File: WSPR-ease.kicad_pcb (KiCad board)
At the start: 4 copper layers, 99 x 64 mm, 113 parts, among them J1 GNSS Ant, J2 Tx Ant, J3 USB_C_16P_Stacked, Q1 MMBF170, Q10 MMBF170, Q11 MMBF170, Q12 MMBF170, Q13 MMBF170, Q2 MMBF170, Q3 MMBF170, Q4 MMBF170, Q5 MMBF170, Q6 MMBF170, Q7 MMBF170, Q8 MMBF170, Q9 MMBF170, T1 BN-43-202_DualPri_CTSec, U1 ESP32-S3-WROOM-1-N8R8, U2 NCP1117-3.3_SOT223, U3 ATGM336H-5N31, U4 ICE40UP5K-SG48ITR, U5 TLV70012, U6 CD74ACT541SM96, U7 SRV05-4

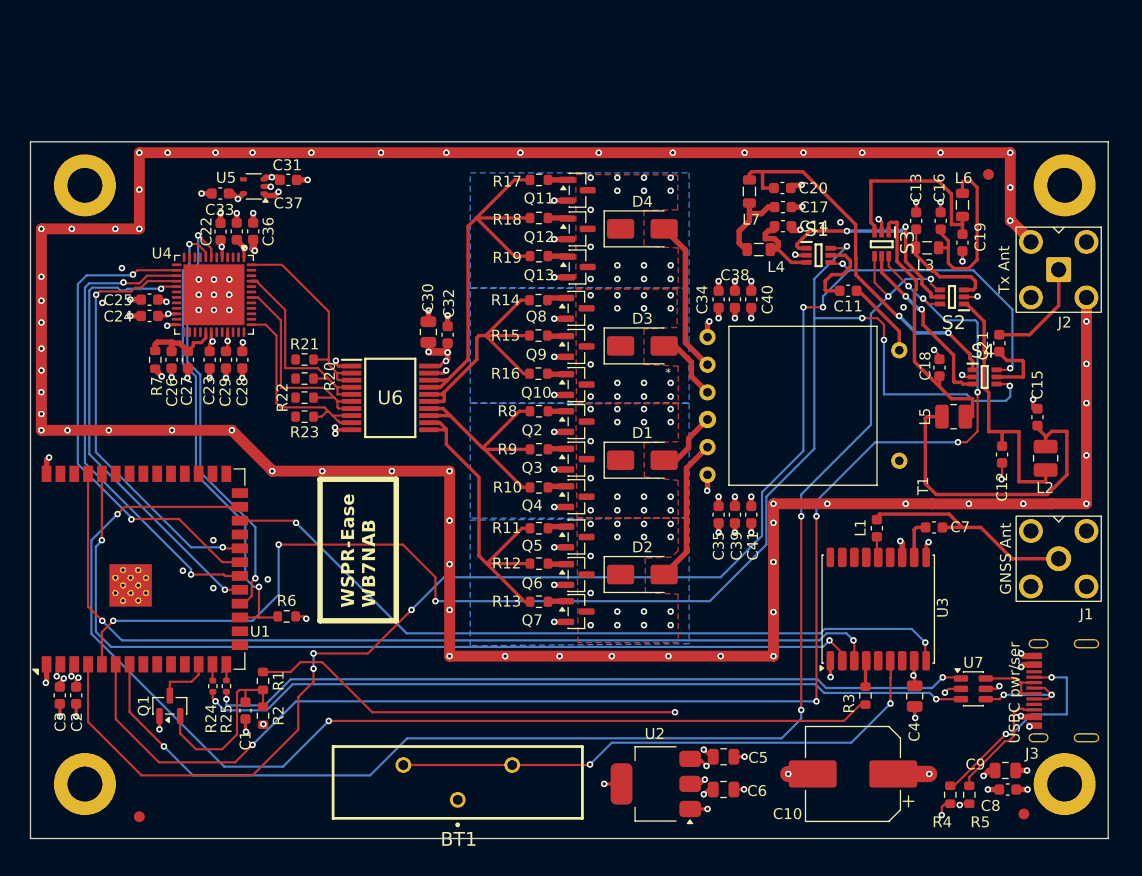
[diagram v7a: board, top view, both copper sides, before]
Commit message: Tarted up, 3d models applied, better footprints and BOM, ready to submit for PCBA
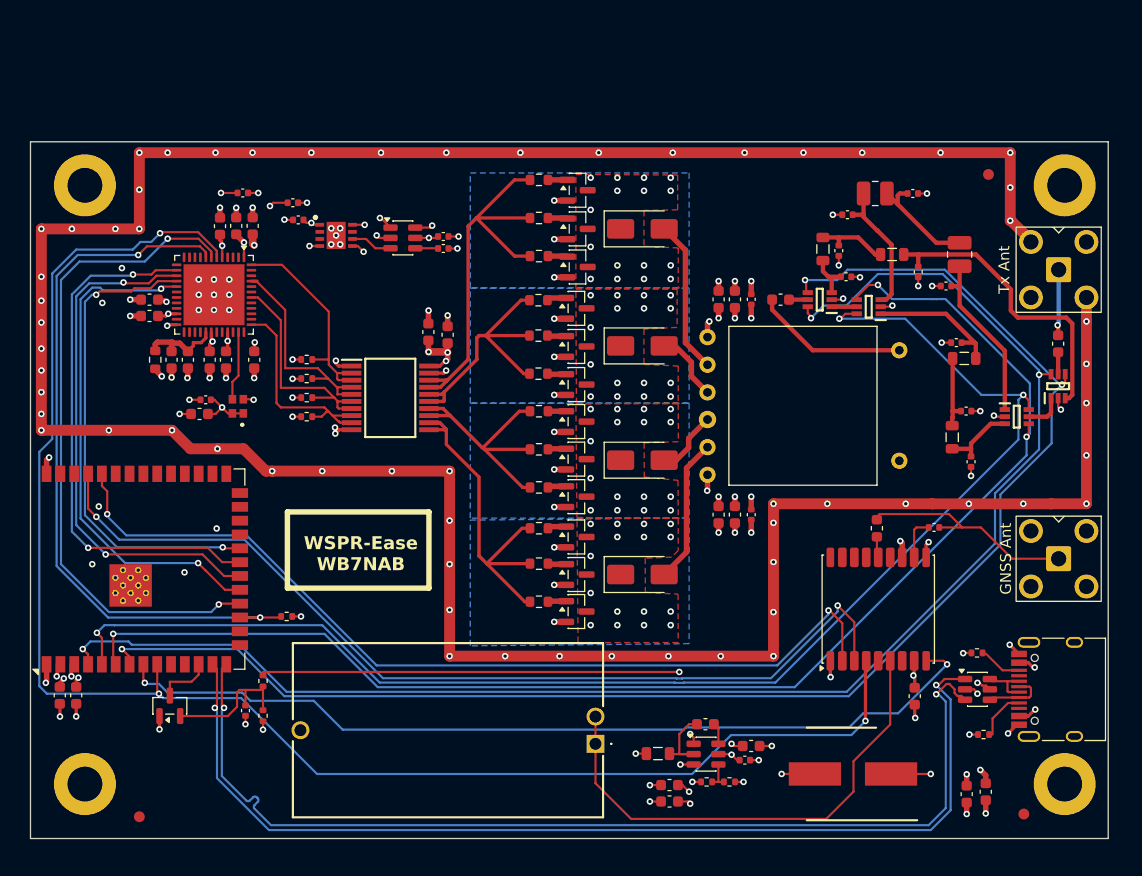
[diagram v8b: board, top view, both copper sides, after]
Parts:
- removed C31, C33: 1uF X7R 25V, Capacitor_SMD:C_0603_1608Metric
- removed C5, C6: 10uF 16V X5R, Capacitor_SMD:C_0805_2012Metric
- removed J3: USB_C_16P_Stacked, Library:HRO-TYPE-C-31-M-12
- removed R24, R25: 0, Resistor_SMD:R_0402_1005Metric
- removed R3: 10k, Resistor_SMD:R_0603_1608Metric
- removed R4, R5: 5.1k, Resistor_SMD:R_0603_1608Metric
- removed U2: NCP1117-3.3_SOT223, Package_TO_SOT_SMD:SOT-223-3_TabPin2
- removed U5: TLV70012, Package_TO_SOT_SMD:SOT-353_SC-70-5
- added C106: 1nF X7R, Capacitor_SMD:C_0402_1005Metric, F.Cu at (87.5, 79.2)
- added C107: 1uF, Capacitor_SMD:C_0402_1005Metric, F.Cu at (74.2, 76.6)
- added C108: 1uF, Capacitor_SMD:C_0402_1005Metric, F.Cu at (87.5, 78.1)
- added C112: 10uF X5R 25V, Capacitor_SMD:C_0603_1608Metric, F.Cu at (115.8, 124.9)
- added C113: 1uF, Capacitor_SMD:C_0402_1005Metric, F.Cu at (115.2, 126.2)
- added C114: 100nF X7R 50V, Capacitor_SMD:C_0603_1608Metric, F.Cu at (111.6, 122.9)
- added C115: 10uF X5R 25V, Capacitor_SMD:C_0603_1608Metric, F.Cu at (108.3, 130.0)
- added C116: 10uF X5R 25V, Capacitor_SMD:C_0603_1608Metric, F.Cu at (108.3, 128.5)
- added C305: 1uF, Capacitor_SMD:C_0402_1005Metric, F.Cu at (65.7, 93.1)
- added C306: 100nF X7R 50V, Capacitor_SMD:C_0603_1608Metric, F.Cu at (65.1, 94.4)
- added C307: 4.7uF, Capacitor_SMD:C_0402_1005Metric, F.Cu at (69.1, 74.1)
- added C310: 4.7uF, Capacitor_SMD:C_0402_1005Metric, F.Cu at (73.7, 75.0)
- added J103: pwr+data, Library:USB_C_Receptacle_HRO_TYPE-C-31-M-12-bursted, F.Cu at (144.4, 119.7)
- added L102: 2.2uH, Inductor_SMD:L_0805_2012Metric, F.Cu at (107.2, 125.6)
- added R103: 5.1k, Resistor_SMD:R_0402_1005Metric, F.Cu at (137.2, 123.8)
- added R104: 5.1k, Resistor_SMD:R_0402_1005Metric, F.Cu at (136.6, 116.3)
- added R105: 100k, Resistor_SMD:R_0402_1005Metric, F.Cu at (111.7, 128.2)
- added R106: 22.1k, Resistor_SMD:R_0402_1005Metric, F.Cu at (113.8, 128.2)
- added U103: TPS22918DBVR, Package_TO_SOT_SMD:SOT-23-6, F.Cu at (83.8, 78.2)
- added U104: TPS74612PQWDRBRQ1, Library:SON65P300X300X100-9N-D, F.Cu at (77.7, 78.0)
- added U106: LMR51430, Package_TO_SOT_SMD:SOT-23-6, F.Cu at (111.7, 125.7)
- added Y301: 40MHz, Library:ECSTXO201633400TR, F.Cu at (68.7, 93.7)
- BT101: renamed from BT1; value S8401-46 -> CR2032 holder; footprint Library:S8401-46 -> Library:BATHLD014THM
- C101: renamed from C4; value 10uF 16V X5R -> 10uF X5R 25V; footprint Capacitor_SMD:C_0805_2012Metric -> Capacitor_SMD:C_0603_1608Metric
- C102: renamed from C1; value 100nF X7R -> 1nF X7R; footprint Capacitor_SMD:C_0603_1608Metric -> Capacitor_SMD:C_0402_1005Metric
- C103: renamed from C7; value 100pF NP0 -> 100pF NP0 50V; footprint Capacitor_SMD:C_0603_1608Metric -> Capacitor_SMD:C_0402_1005Metric
- C104: renamed from C2; value 100nF X7R -> 100nF X7R 50V
- C105: renamed from C3; value 10uF X5R -> 10uF X5R 25V
- C109: renamed from C10; footprint Capacitor_SMD:CP_Elec_8x10.5 -> Library:CAPAE850X1050N
- C110: renamed from C9; value 10uF 16V X5R -> 10uF X5R 25V; footprint Capacitor_SMD:C_0805_2012Metric -> Capacitor_SMD:C_0603_1608Metric
- C201: renamed from C11; value 100nF X7R -> 100nF X7R 50V
- C202: renamed from C12; footprint Capacitor_SMD:C_0603_1608Metric -> Capacitor_SMD:C_0402_1005Metric
- C203: renamed from C13; footprint Capacitor_SMD:C_0603_1608Metric -> Capacitor_SMD:C_0402_1005Metric
- C204: renamed from C14; value 100pF NP0 -> 100pF NP0 50V; footprint Capacitor_SMD:C_0603_1608Metric -> Capacitor_SMD:C_0402_1005Metric
- C205: renamed from C15; footprint Capacitor_SMD:C_0603_1608Metric -> Capacitor_SMD:C_0402_1005Metric
- C206: renamed from C16; footprint Capacitor_SMD:C_0603_1608Metric -> Capacitor_SMD:C_0402_1005Metric
- C207: renamed from C17; footprint Capacitor_SMD:C_0603_1608Metric -> Capacitor_SMD:C_0402_1005Metric
- C208: renamed from C18; footprint Capacitor_SMD:C_0603_1608Metric -> Capacitor_SMD:C_0402_1005Metric
- C209: renamed from C19; footprint Capacitor_SMD:C_0603_1608Metric -> Capacitor_SMD:C_0402_1005Metric
- C210: renamed from C20; value 100pF NP0 -> 100pF NP0 50V; footprint Capacitor_SMD:C_0603_1608Metric -> Capacitor_SMD:C_0402_1005Metric
- C211: renamed from C21; value 100nF X7R -> 100nF X7R 50V
- C301: renamed from C28; value 100nF X7R -> 100nF X7R 50V
- C302: renamed from C29; value 10uF X5R -> 10uF X5R 25V
- C303: renamed from C36; value 100nF X7R -> 100nF X7R 50V
- C304: renamed from C37; value 10uF X5R -> 10uF X5R 25V
- C308: renamed from C30; value 10uF 16V X5R -> 10uF X5R 25V; footprint Capacitor_SMD:C_0805_2012Metric -> Capacitor_SMD:C_0603_1608Metric
- C309: renamed from C32; value 100nF X7R -> 100nF X7R 50V
- C311: renamed from C24; value 100nF X7R -> 100nF X7R 50V
- C312: renamed from C25; value 10uF X5R -> 10uF X5R 25V
- C313: renamed from C22; value 100nF X7R -> 100nF X7R 50V
- C314: renamed from C23; value 10uF X5R -> 10uF X5R 25V
- C315: renamed from C34; value 10uF X7R 25V -> 10uF X5R 25V
- C316: renamed from C35; value 10uF X7R 25V -> 10uF X5R 25V
- C319: renamed from C40; footprint Capacitor_SMD:C_0603_1608Metric -> Capacitor_SMD:C_0402_1005Metric
- C320: renamed from C41; footprint Capacitor_SMD:C_0603_1608Metric -> Capacitor_SMD:C_0402_1005Metric
- C321: renamed from C26; value 100nF X7R -> 100nF X7R 50V
- C322: renamed from C27; value 10uF X5R -> 10uF X5R 25V
- R101: renamed from R1; footprint Resistor_SMD:R_0603_1608Metric -> Resistor_SMD:R_0402_1005Metric
- R102: renamed from R2; footprint Resistor_SMD:R_0603_1608Metric -> Resistor_SMD:R_0402_1005Metric
- R301: renamed from R6; footprint Resistor_SMD:R_0603_1608Metric -> Resistor_SMD:R_0402_1005Metric
- R302: renamed from R20; footprint Resistor_SMD:R_0603_1608Metric -> Resistor_SMD:R_0402_1005Metric
- R303: renamed from R21; footprint Resistor_SMD:R_0603_1608Metric -> Resistor_SMD:R_0402_1005Metric
- R304: renamed from R22; footprint Resistor_SMD:R_0603_1608Metric -> Resistor_SMD:R_0402_1005Metric
- R305: renamed from R23; footprint Resistor_SMD:R_0603_1608Metric -> Resistor_SMD:R_0402_1005Metric
- moved L201 28.9 mm to (127.2, 74.2), turned to 0 degrees
- moved C202 26.2 mm to (124.7, 76.1), turned to 180 degrees
- moved C205 23.5 mm to (130.7, 74.2), turned to 0 degrees
- moved L205 21.4 mm to (134.3, 96.5)
- moved C209 20.1 mm to (136.0, 98.8)
- moved U203 20.1 mm to (140.2, 94.7), turned to 0 degrees
- moved C206 17.6 mm to (135.6, 94.1), turned to 0 degrees
- moved L204 14.9 mm to (134.9, 79.8), turned to -90 degrees
- moved C210 14.7 mm to (131.2, 81.3), turned to -90 degrees
- moved L206 14.3 mm to (128.8, 79.8), turned to 0 degrees
- moved BT101 13.1 mm to (101.5, 124.7)
- moved C203 11.8 mm to (134.7, 87.8), turned to 180 degrees
- moved L202 10.7 mm to (135.4, 89.3), turned to 180 degrees
- moved U202 7.70 mm to (126.6, 84.5)
- moved C208 7.52 mm to (133.7, 82.7), turned to 180 degrees
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- renumbered C8 to C111, C38 to C317, C39 to C318, D1 to D301, D2 to D302, D3 to D303, D4 to D304, FID3 to FID101, FID2 to FID102, FID1 to FID103, H1 to H101, H2 to H102, H3 to H103, H4 to H104, J1 to J101, J2 to J102, L1 to L101, L2 to L201, L3 to L202, L4 to L203, L5 to L204, L6 to L205, L7 to L206, Q1 to Q101, Q2 to Q301, Q3 to Q302, Q4 to Q303, Q5 to Q304, Q6 to Q305, Q7 to Q306, Q8 to Q307, Q9 to Q308, Q10 to Q309, Q11 to Q310, Q12 to Q311, Q13 to Q312, R8 to R306, R9 to R307, R10 to R308, R11 to R309, R12 to R310, R13 to R311, R14 to R312, R15 to R313, R16 to R314, R17 to R315, R18 to R316, R19 to R317, R7 to R318, T1 to T301, U3 to U101, U1 to U102, U7 to U105, S1 to U201, S2 to U202, S3 to U203, S4 to U204, U4 to U301, U6 to U302
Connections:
- net +1V2 renamed +VFPGACORE
- BT101 pad 1: GND -> Net-(BT101-+_1)
- BT101 pad 2: Net-(U3-V_BCKP) -> Net-(BT101-+_1)
- BT101 pad 3: Net-(U3-V_BCKP) -> GND
- C202 pad 1: Net-(S2-J2) -> Net-(U202-J3)
- C203 pad 1: Net-(S2-J3) -> Net-(U202-J2)
- C210 pad 1: Net-(S4-J2) -> Net-(U204-J3)
- C301 pad 2: +3.3V -> +VFPGAIO
- C302 pad 2: +3.3V -> +VFPGAIO
- C303 pad 2: +3.3V -> +VFPGAIO
- C304 pad 2: +3.3V -> +VFPGAIO
- C308 pad 2: +3.3V -> +VFPGAIO
- C309 pad 2: +3.3V -> +VFPGAIO
- C311 pad 2: +3.3V -> +VFPGAIO
- C312 pad 2: +3.3V -> +VFPGAIO
- L201 pad 1: Net-(S2-J2) -> Net-(U202-J3)
- L202 pad 1: Net-(S2-J3) -> Net-(U202-J2)
- L206 pad 2: Net-(S4-J2) -> Net-(U204-J3)
- U101 pad 6: Net-(U3-V_BCKP) -> Net-(BT101-+_1)
- U102 pad 13: Net-(U1-USB_D-) -> /D+
- U102 pad 14: Net-(U1-USB_D+) -> /D-
- U102 pad 24: /gnssNRESET -> unconnected-(U102-IO47-Pad24)
- U102 pad 25: Net-(U1-IO48) -> unconnected-(U102-IO48-Pad25)
- U102 pad 4: /hiON -> /loON
- U102 pad 5: /loON -> /lo1ON
- U102 pad 6: /lo1ON -> /lo2ON
- U102 pad 7: /lo2ON -> /hiON
- U102 pad 8: unconnected-(U1-IO15-Pad8) -> /gnssNRESET
- U102 pad 9: unconnected-(U1-IO16-Pad9) -> /gnssPPS
- U202 pad 1: Net-(S2-J2) -> Net-(U202-J2)
- U202 pad 3: Net-(S2-J3) -> Net-(U202-J3)
- U203 pad 5: Net-(S3-J1) -> Net-(U203-J1)
- U204 pad 1: Net-(S4-J2) -> Net-(U203-J1)
- U204 pad 3: Net-(S3-J1) -> Net-(U204-J3)
- U204 pad 4: /loON -> /hiON
- U204 pad 6: /hiON -> /loON
- U301 pad 1: +3.3V -> +VFPGAIO
- U301 pad 22: +3.3V -> +VFPGAIO
- U301 pad 33: +3.3V -> +VFPGAIO
- U301 pad 35: unconnected-(U4A-IOT_46b_G0-Pad35) -> /Transmitter/FPGACLK
- U301 pad 6: unconnected-(U4B-IOB_13b-Pad6) -> /gnssPPS
- U302 pad 20: +3.3V -> +VFPGAIO
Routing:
- net /gnssPPS: track 2.41 -> 145.9 mm, vias 0 -> 3
- net Net-(U1-IO48): track 101.7 -> 0.00 mm, vias 2 -> 0
- net Net-(U3-V_BCKP): track 50.7 -> 0.00 mm, vias 2 -> 0
- net Net-(BT101-+_1): track 0.00 -> 45.6 mm
- net Net-(S4-J2): track 34.6 -> 0.00 mm, vias 2 -> 0
- net Net-(U204-J3): track 0.00 -> 27.7 mm
- net /D+: track 70.5 -> 95.8 mm
- net Net-(S2-J2): track 25.2 -> 0.00 mm
- net /D-: track 71.4 -> 95.7 mm
- net +VFPGAIO: track 0.00 -> 24.2 mm, vias 0 -> 13
- net /fpgaNRESET: track 43.8 -> 66.5 mm
- net /fpgaDONE: track 41.2 -> 61.1 mm
- net Net-(J3-CC1): track 19.8 -> 0.00 mm, vias 2 -> 0
- net Net-(C205-Pad1): track 30.1 -> 10.3 mm
- net Net-(U201-J2): track 20.0 -> 2.30 mm, vias 2 -> 0
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- added copper zone on In2.Cu, net +VFPGAIO
